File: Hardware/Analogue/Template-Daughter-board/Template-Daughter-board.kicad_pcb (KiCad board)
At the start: 2 copper layers, 140.3 x 65 mm, 10 parts, among them J1 Audio In, J2 Audio Out, J3 Digital Pass Through, J4 Digital In, J5 Power Out, J6 Power In

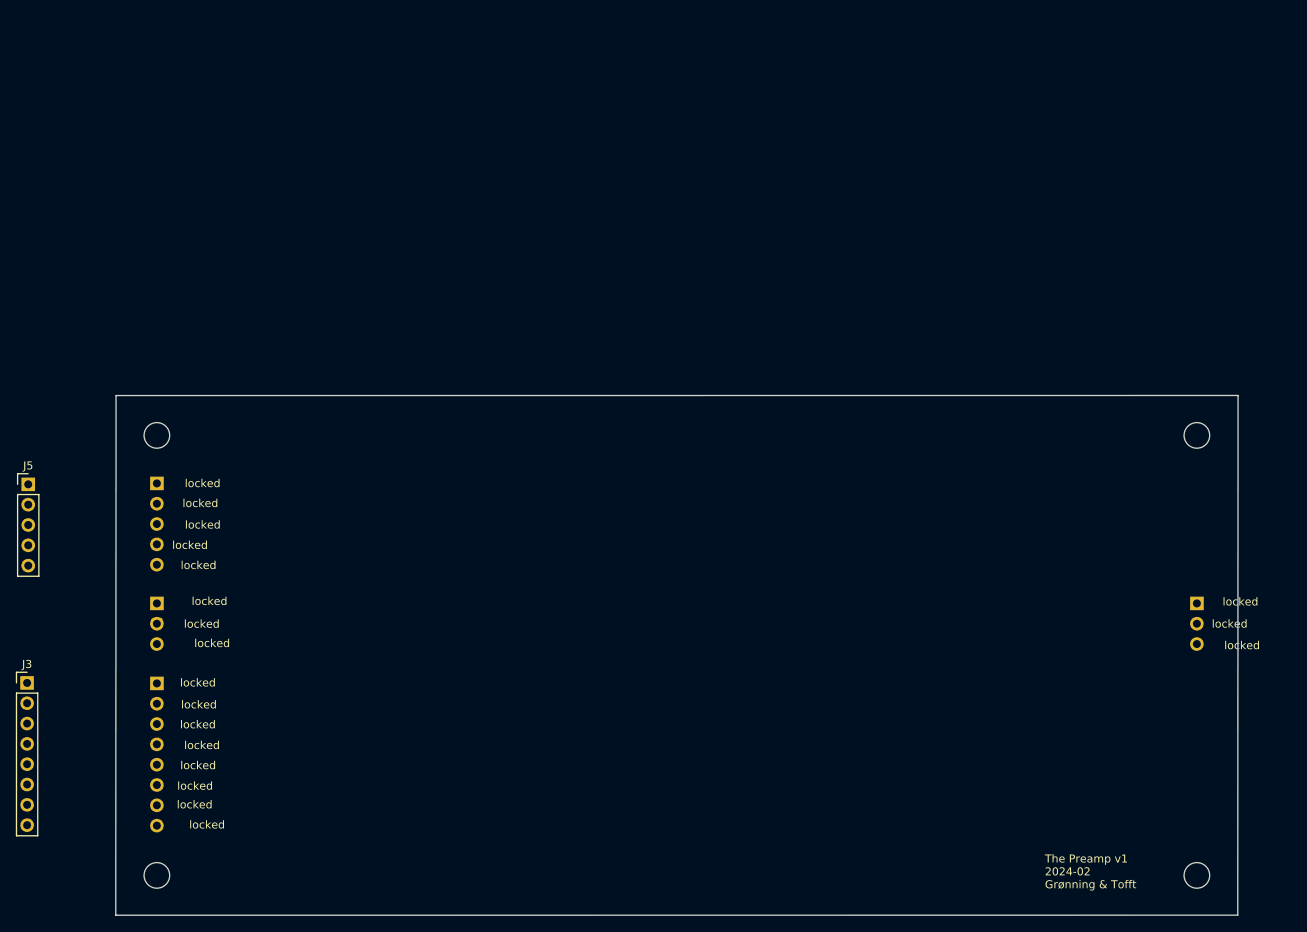
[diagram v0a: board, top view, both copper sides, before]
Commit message: Updated Template-Daughter-board to reflect changes
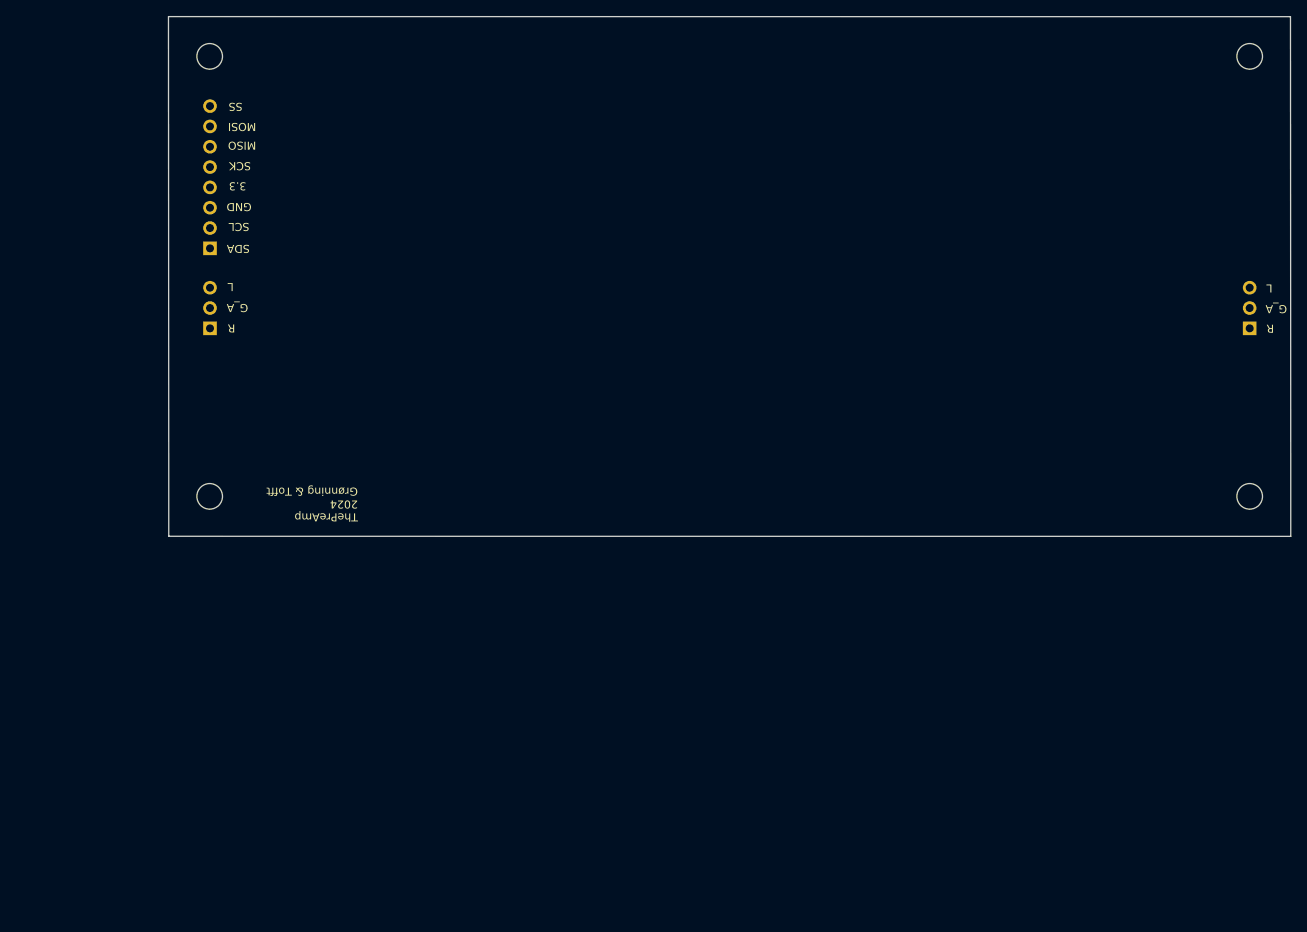
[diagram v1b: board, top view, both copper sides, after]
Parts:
- removed J3: Digital Pass Through, Connector_PinHeader_2.54mm:PinHeader_1x08_P2.54mm_Vertical
- removed J5: Power Out, Connector_PinHeader_2.54mm:PinHeader_1x05_P2.54mm_Vertical
- removed J6: Power In, Connector_PinHeader_2.54mm:PinHeader_1x05_P2.54mm_Vertical
- moved REF** 170.7 mm to (221.9, 32.2), turned to 180 degrees
- moved REF** 160.3 mm to (91.9, 32.2), turned to 180 degrees
- moved REF** 136.8 mm to (221.9, 87.2), turned to 180 degrees
- moved REF** 123.6 mm to (91.9, 87.2), turned to 180 degrees
- moved J4 54.8 mm to (91.9, 56.2), turned to 0 degrees
- moved J1 35.0 mm to (91.9, 66.2), turned to 0 degrees
- moved J2 35.0 mm to (221.9, 66.2), turned to 0 degrees
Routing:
- net GNDA: track 1.26 -> 0.00 mm
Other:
- outline, holes or cut-outs redrawn
- board text added: "3.3"
- board text added: "GND"
- board text added: "G_A"
- board text added: "L"
- board text added: "MISO"
- board text added: "MOSI"
- board text added: "R"
- board text added: "SCK"
- board text added: "SCL"
- board text added: "SDA"
- board text added: "SS"
- board text added: "ThePreAmp 2024 Grønning & Tofft"
- board text added: "This PCB is shown upside-down to have input on the left side and output on the right"
- board text removed: "The Preamp v1 2024-02 Grønning & Tofft"
- board text removed: "locked"
